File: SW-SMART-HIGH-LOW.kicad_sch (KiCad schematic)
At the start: 31 parts, among them IC1 MCP1416, J1 1 CTL IN, SW1 BTS50010-1TAD, SW2 VNB35N07xx-E, U1 STM32G071K8TxN, U2 NCV1117ST50, U3 NCV1117ST33, U4 MCP2562-E-SN

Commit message: fit a lot of stuff onto a small board
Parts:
- removed J1: 1 CTL IN, Connector_PinHeader_2.54mm:PinHeader_1x05_P2.54mm_Horizontal, symbol Connector_Generic:Conn_01x05
- removed U1: STM32G071K8TxN, Package_QFP:LQFP-32_7x7mm_P0.8mm, symbol MCU_ST_STM32G0:STM32G071K8TxN
- added CNRST1, CSTM2: 100n, Capacitor_SMD:C_0603_1608Metric_Pad1.08x0.95mm_HandSolder, symbol Device:C_Small
- added CSTM1: 4u7, Capacitor_SMD:C_0805_2012Metric_Pad1.18x1.45mm_HandSolder, symbol Device:C_Small
- added J1: H GND L, TerminalBlock_Phoenix:TerminalBlock_Phoenix_MKDS-1,5-3-5.08_1x03_P5.08mm_Horizontal, symbol Connector:Screw_Terminal_01x03
- added J2: SWLINK, symbol Connector_Generic:Conn_01x05
- added U1: STM32G0B1KBTx, Package_QFP:LQFP-32_7x7mm_P0.8mm, symbol MCU_ST_STM32G0:STM32G0B1KBTx
- renumbered RPD1 to R1
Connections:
- net +3.3V: now also CSTM1.1, CSTM2.1, J2.1 (Pin_1), U1.4 (VDD)
- net GND: now also CNRST1.2, CSTM1.2, CSTM2.2, J1.2 (Pin_2), J2.5 (Pin_5), U1.5 (VSS)
- net LOW_IN: no longer RIN2.1
- net SW1IN: no longer RIN1.1
- net SW1IS: no longer RIS_PROT1.1
- net CAN1_TX: now reaches U4.1 (TXD)
- net CAN1_TX: now also U1.23 (PA10/PA12)
- net CAN1_RX: now reaches U4.4 (RXD)
- net CAN1_RX: now also U1.22 (PA9/PA11)
- net CAN_L: now reaches U4.6 (CANL)
- net CAN_L: now also J1.3 (Pin_3)
- net CAN_H: now reaches U4.7 (CANH)
- net CAN_H: now also J1.1 (Pin_1)
- new net NRST: CNRST1.1, J2.2 (Pin_2), U1.6 (PF2)
- new net SWCLK: J2.3 (Pin_3), U1.25 (PA14)
- new net SWDIO: J2.4 (Pin_4), U1.24 (PA13)
- new net USART1_RX: U1.21 (PA10/UCPD1_DBCC2)
- new net USART1_TX: U1.19 (PA9/UCPD1_DBCC1)
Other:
- moved on the sheet: C3V1, C5V0, C5V1, U2, U3

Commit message: making progress on the layout
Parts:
- J1: renamed from J2; footprint (none) -> PCM_SparkFun-Connector:1x05_P2.54mm_Locking
- renumbered J1 to CAN1, U3 to VR3V3, U2 to VR5V0
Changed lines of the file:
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@@
 		(dnp no)
 		(fields_autoplaced yes)
-		(property "Reference" "J1"
+		(property "Reference" "CAN1"
 			(at 251.46 97.7899 0)
 			(effects
@@
 			(project ""
 				(path "/08d9f551-d314-4c5c-859f-da02a807087d"
-					(reference "J1")
+					(reference "CAN1")
 					(unit 1)
 				)
@@
 		(dnp no)
 		(fields_autoplaced yes)
-		(property "Reference" "U2"
+		(property "Reference" "VR5V0"
 			(at 38.1 69.85 0)
 			(effects
@@
 			(project ""
 				(path "/08d9f551-d314-4c5c-859f-da02a807087d"
-					(reference "U2")
+					(reference "VR5V0")
 					(unit 1)
 				)
@@
 		(dnp no)
 		(fields_autoplaced yes)
-		(property "Reference" "J2"
+		(property "Reference" "J1"
 			(at 248.92 26.6699 0)
 			(effects
@@
 			)
 		)
-		(property "Footprint" ""
+		(property "Footprint" "PCM_SparkFun-Connector:1x05_P2.54mm_Locking"
 			(at 246.38 27.94 0)
 			(effects
@@
 			(project ""
 				(path "/08d9f551-d314-4c5c-859f-da02a807087d"
-					(reference "J2")
+					(reference "J1")
 					(unit 1)
 				)
@@
 		(dnp no)
 		(fields_autoplaced yes)
-		(property "Reference" "U3"
+		(property "Reference" "VR3V3"
 			(at 71.12 69.85 0)
 			(effects
@@
 			(project ""
 				(path "/08d9f551-d314-4c5c-859f-da02a807087d"
-					(reference "U3")
-					(unit 1)
-				)
+					(reference "VR3V3")
+					(unit 1)
+				)

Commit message: needs a bit more work
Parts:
- added J2: USART1, PCM_SparkFun-Connector:1x04_P2.54mm_Locking, symbol Connector_Generic:Conn_01x04
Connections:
- net +3.3V: now also J2.1 (Pin_1)
- net GND: now also J2.4 (Pin_4)
- net USART1_RX: now also J2.3 (Pin_3)
- net USART1_TX: now also J2.2 (Pin_2)
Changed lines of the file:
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@@
 	)
 	(junction
+		(at 223.52 99.06)
+		(diameter 0)
+		(color 0 0 0 0)
+	)
+	(junction
 		(at 92.71 49.53)
 		(diameter 0)
@@
 	(wire
 		(pts
+			(xy 223.52 87.63) (xy 223.52 99.06)
+		)
+		(stroke
+			(width 0)
+			(type default)
+		)
+	)
+	(wire
+		(pts
 			(xy 248.92 114.3) (xy 248.92 124.46)
 		)
@@
 	(wire
 		(pts
+			(xy 241.3 85.09) (xy 243.84 85.09)
+		)
+		(stroke
+			(width 0)
+			(type default)
+		)
+	)
+	(wire
+		(pts
 			(xy 116.84 66.04) (xy 101.6 66.04)
 		)
@@
 	(wire
 		(pts
+			(xy 243.84 87.63) (xy 223.52 87.63)
+		)
+		(stroke
+			(width 0)
+			(type default)
+		)
+	)
+	(wire
+		(pts
 			(xy 213.36 71.12) (xy 217.17 71.12)
 		)
@@
 	(wire
 		(pts
+			(xy 241.3 82.55) (xy 243.84 82.55)
+		)
+		(stroke
+			(width 0)
+			(type default)
+		)
+	)
+	(wire
+		(pts
 			(xy 25.4 96.52) (xy 38.1 96.52)
 		)
@@
 	(wire
 		(pts
-			(xy 187.96 99.06) (xy 243.84 99.06)
+			(xy 243.84 80.01) (xy 242.57 80.01)
+		)
+		(stroke
+			(width 0)
+			(type default)
+		)
+	)
+	(wire
+		(pts
+			(xy 187.96 99.06) (xy 223.52 99.06)
 		)
 		(stroke
@@
 	(wire
 		(pts
+			(xy 223.52 99.06) (xy 243.84 99.06)
+		)
+		(stroke
+			(width 0)
+			(type default)
+		)
+	)
+	(wire
+		(pts
 			(xy 92.71 49.53) (xy 92.71 60.96)
 		)
@@
 	(wire
 		(pts
+			(xy 242.57 76.2) (xy 242.57 80.01)
+		)
+		(stroke
+			(width 0)
+			(type default)
+		)
+	)
+	(wire
+		(pts
 			(xy 69.85 115.57) (xy 74.93 115.57)
 		)
@@
 		)
 	)
+	(label "USART1_RX"
+		(at 241.3 85.09 180)
+		(effects
+			(font
+				(size 1.27 1.27)
+			)
+			(justify right bottom)
+		)
+	)
 	(label "CAN_H"
 		(at 240.03 96.52 180)
@@
 		)
 	)
+	(label "USART1_TX"
+		(at 241.3 82.55 180)
+		(effects
+			(font
+				(size 1.27 1.27)
+			)
+			(justify right bottom)
+		)
+	)
 	(label "NRST"
 		(at 156.21 40.64 180)
@@
 	)
 	(symbol
+		(lib_id "Connector_Generic:Conn_01x04")
+		(at 248.92 82.55 0)
+		(unit 1)
+		(exclude_from_sim no)
+		(in_bom yes)
+		(on_board yes)
+		(dnp no)
+		(fields_autoplaced yes)
+		(property "Reference" "J2"
+			(at 251.46 82.5499 0)
+			(effects
+				(font
+					(size 1.27 1.27)
+				)
+				(justify left)
+			)
+		)
+		(property "Value" "USART1"
+			(at 251.46 85.0899 0)
+			(effects
+				(font
+					(size 1.27 1.27)
+				)
+				(justify left)
+			)
+		)
+		(property "Footprint" "PCM_SparkFun-Connector:1x04_P2.54mm_Locking"
+			(at 248.92 82.55 0)
+			(effects
+				(font
+					(size 1.27 1.27)
+				)
+				(hide yes)
+			)
+		)
+		(property "Datasheet" "~"
+			(at 248.92 82.55 0)
+			(effects
+				(font
+					(size 1.27 1.27)
+				)
+				(hide yes)
+			)
+		)
+		(property "Description" "Generic connector, single row, 01x04, script generated (kicad-library-utils/schlib/autogen/connector/)"
+			(at 248.92 82.55 0)
+			(effects
+				(font
+					(size 1.27 1.27)
+				)
+				(hide yes)
+			)
+		)
+		(pin "2"
+		)
+		(pin "4"
+		)
+		(pin "1"
+		)
+		(pin "3"
+		)
+		(instances
+			(project ""
+				(path "/08d9f551-d314-4c5c-859f-da02a807087d"
+					(reference "J2")
+					(unit 1)
+				)
+			)
+		)
+	)
+	(symbol
 		(lib_id "power:GND")
 		(at 187.96 102.87 0)
@@
 					(unit 1)
 				)
+			)
+		)
+	)
+	(symbol
+		(lib_id "power:+3.3V")
+		(at 242.57 76.2 0)
+		(unit 1)
+		(exclude_from_sim no)
+		(in_bom yes)
+		(on_board yes)
+		(dnp no)
+		(fields_autoplaced yes)
+		(property "Reference" "#PWR021"
+			(at 242.57 80.01 0)
+			(effects
+				(font
+					(size 1.27 1.27)
+				)
+				(hide yes)
+			)
+		)
+		(property "Value" "+3.3V"
+			(at 242.57 71.12 0)
+			(effects
+				(font
+					(size 1.27 1.27)
+				)
+			)
+		)
+		(property "Footprint" ""
+			(at 242.57 76.2 0)
+			(effects
+				(font
+					(size 1.27 1.27)
+				)
+				(hide yes)
+			)
+		)
+		(property "Datasheet" ""
+			(at 242.57 76.2 0)
+			(effects
+				(font
+					(size 1.27 1.27)
+				)
+				(hide yes)
+			)
+		)
+		(property "Description" "Power symbol creates a global label with name \"+3.3V\""
+			(at 242.57 76.2 0)
+			(effects
+				(font
+					(size 1.27 1.27)
+				)
+				(hide yes)
+			)
+		)
+		(pin "1"
+		)
+		(instances
+			(project "SW-SMART-HIGH-LOW"
+				(path "/08d9f551-d314-4c5c-859f-da02a807087d"
+					(reference "#PWR021")
+					(unit 1)
+				)

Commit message: added voltage divider for +12v
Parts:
- added CDIV1, CIS1: 100n, Capacitor_SMD:C_0603_1608Metric_Pad1.08x0.95mm_HandSolder, symbol Device:C_Small
- added RVDIV1: 10K, Resistor_SMD:R_0603_1608Metric_Pad0.98x0.95mm_HandSolder, symbol Device:R_Small_US
- added RVDIV2: 4K7, Resistor_SMD:R_0603_1608Metric_Pad0.98x0.95mm_HandSolder, symbol Device:R_Small_US
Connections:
- net +12V: now also RVDIV1.2
- net GND: now also CDIV1.2, CIS1.2, RVDIV2.1
- net SW1IN: now also RIN1.1, U1.32 (PB8)
- net SW1IS: now also RIS_PROT1.1, U1.7 (PA0), CIS1.1
- net SW2IN: now reaches RIN2.1
- net SW2IN: now also U1.30 (PB6)
- net VS: now reaches U1.9 (PA2)
- net VS: now also CDIV1.1, RVDIV1.1, RVDIV2.2

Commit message: I think the layout is complete
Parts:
- renumbered R1 to RSTBY1
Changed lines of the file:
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@@
 		(on_board yes)
 		(dnp no)
-		(property "Reference" "R1"
+		(property "Reference" "RSTBY1"
 			(at 113.538 83.312 0)
 			(effects
@@
 			(project "SW-SMART-HIGH-LOW"
 				(path "/08d9f551-d314-4c5c-859f-da02a807087d"
-					(reference "R1")
+					(reference "RSTBY1")
 					(unit 1)
 				)

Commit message: added caps for gate drive IC
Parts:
- added CFET1: 100n, Capacitor_SMD:C_0603_1608Metric_Pad1.08x0.95mm_HandSolder, symbol Device:C_Small
- added CFET2: 1u, Capacitor_SMD:C_0805_2012Metric_Pad1.18x1.45mm_HandSolder, symbol Device:C_Small
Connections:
- net +12V: now also CFET1.1, CFET2.1
- net GND: now also CFET1.2, CFET2.2
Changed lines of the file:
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@@
 	)
 	(junction
+		(at 21.59 60.96)
+		(diameter 0)
+		(color 0 0 0 0)
+	)
+	(junction
 		(at 62.23 38.1)
 		(diameter 0)
@@
 	)
 	(junction
+		(at 21.59 38.1)
+		(diameter 0)
+		(color 0 0 0 0)
+	)
+	(junction
 		(at 92.71 29.21)
 		(diameter 0)
@@
 	)
 	(junction
+		(at 33.02 60.96)
+		(diameter 0)
+		(color 0 0 0 0)
+	)
+	(junction
 		(at 92.71 46.99)
 		(diameter 0)
@@
 	)
 	(junction
+		(at 33.02 38.1)
+		(diameter 0)
+		(color 0 0 0 0)
+	)
+	(junction
 		(at 123.19 22.86)
 		(diameter 0)
@@
 	(wire
 		(pts
+			(xy 21.59 38.1) (xy 21.59 45.72)
+		)
+		(stroke
+			(width 0)
+			(type default)
+		)
+	)
+	(wire
+		(pts
 			(xy 57.15 87.63) (xy 57.15 96.52)
 		)
@@
 	(wire
 		(pts
+			(xy 33.02 60.96) (xy 21.59 60.96)
+		)
+		(stroke
+			(width 0)
+			(type default)
+		)
+	)
+	(wire
+		(pts
 			(xy 160.02 132.08) (xy 160.02 135.89)
 		)
@@
 	(wire
 		(pts
+			(xy 17.78 38.1) (xy 17.78 40.64)
+		)
+		(stroke
+			(width 0)
+			(type default)
+		)
+	)
+	(wire
+		(pts
 			(xy 62.23 49.53) (xy 69.85 49.53)
 		)
@@
 	(wire
 		(pts
+			(xy 21.59 50.8) (xy 21.59 60.96)
+		)
+		(stroke
+			(width 0)
+			(type default)
+		)
+	)
+	(wire
+		(pts
 			(xy 236.22 25.4) (xy 241.3 25.4)
 		)
@@
 	(wire
 		(pts
+			(xy 21.59 60.96) (xy 17.78 60.96)
+		)
+		(stroke
+			(width 0)
+			(type default)
+		)
+	)
+	(wire
+		(pts
 			(xy 233.68 146.05) (xy 248.92 146.05)
 		)
@@
 	(wire
 		(pts
+			(xy 33.02 38.1) (xy 21.59 38.1)
+		)
+		(stroke
+			(width 0)
+			(type default)
+		)
+	)
+	(wire
+		(pts
 			(xy 48.26 73.66) (xy 48.26 81.28)
 		)
@@
 	(wire
 		(pts
+			(xy 21.59 38.1) (xy 17.78 38.1)
+		)
+		(stroke
+			(width 0)
+			(type default)
+		)
+	)
+	(wire
+		(pts
 			(xy 105.41 177.8) (xy 105.41 182.88)
 		)
@@
 	(wire
 		(pts
+			(xy 17.78 60.96) (xy 17.78 45.72)
+		)
+		(stroke
+			(width 0)
+			(type default)
+		)
+	)
+	(wire
+		(pts
 			(xy 113.03 109.22) (xy 113.03 113.03)
 		)
@@
 	)
 	(symbol
+		(lib_id "Device:C_Small")
+		(at 17.78 43.18 0)
+		(unit 1)
+		(exclude_from_sim no)
+		(in_bom yes)
+		(on_board yes)
+		(dnp no)
+		(fields_autoplaced yes)
+		(property "Reference" "CFET2"
+			(at 20.32 41.9162 0)
+			(effects
+				(font
+					(size 1.27 1.27)
+				)
+				(justify left)
+			)
+		)
+		(property "Value" "1u"
+			(at 20.32 44.4562 0)
+			(effects
+				(font
+					(size 1.27 1.27)
+				)
+				(justify left)
+			)
+		)
+		(property "Footprint" "Capacitor_SMD:C_0805_2012Metric_Pad1.18x1.45mm_HandSolder"
+			(at 17.78 43.18 0)
+			(effects
+				(font
+					(size 1.27 1.27)
+				)
+				(hide yes)
+			)
+		)
+		(property "Datasheet" "~"
+			(at 17.78 43.18 0)
+			(effects
+				(font
+					(size 1.27 1.27)
+				)
+				(hide yes)
+			)
+		)
+		(property "Description" "Low ESR film"
+			(at 17.78 43.18 0)
+			(effects
+				(font
+					(size 1.27 1.27)
+				)
+				(hide yes)
+			)
+		)
+		(pin "2"
+		)
+		(pin "1"
+		)
+		(instances
+			(project "SW-SMART-HIGH-LOW"
+				(path "/08d9f551-d314-4c5c-859f-da02a807087d"
+					(reference "CFET2")
+					(unit 1)
+				)
+			)
+		)
+	)
+	(symbol
 		(lib_id "Connector_Generic:Conn_01x05")
 		(at 246.38 27.94 0)
@@
 					(unit 1)
 				)
+			)
+		)
+	)
+	(symbol
+		(lib_id "Device:C_Small")
+		(at 21.59 48.26 0)
+		(unit 1)
+		(exclude_from_sim no)
+		(in_bom yes)
+		(on_board yes)
+		(dnp no)
+		(fields_autoplaced yes)
+		(property "Reference" "CFET1"
+			(at 24.13 46.9962 0)
+			(effects
+				(font
+					(size 1.27 1.27)
+				)
+				(justify left)
+			)
+		)
+		(property "Value" "100n"
+			(at 24.13 49.5362 0)
+			(effects
+				(font
+					(size 1.27 1.27)
+				)
+				(justify left)
+			)
+		)
+		(property "Footprint" "Capacitor_SMD:C_0603_1608Metric_Pad1.08x0.95mm_HandSolder"
+			(at 21.59 48.26 0)
+			(effects
+				(font
+					(size 1.27 1.27)
+				)
+				(hide yes)
+			)
+		)
+		(property "Datasheet" "~"
+			(at 21.59 48.26 0)
+			(effects
+				(font
+					(size 1.27 1.27)
+				)
+				(hide yes)
+			)
+		)
+		(property "Description" "Unpolarized capacitor, small symbol"
+			(at 21.59 48.26 0)
+			(effects
+				(font
+					(size 1.27 1.27)
+				)
+				(hide yes)
+			)
+		)
+		(pin "2"
+		)
+		(pin "1"
+		)
+		(instances
+			(project "SW-SMART-HIGH-LOW"
+				(path "/08d9f551-d314-4c5c-859f-da02a807087d"
+					(reference "CFET1")
+					(unit 1)
+				)

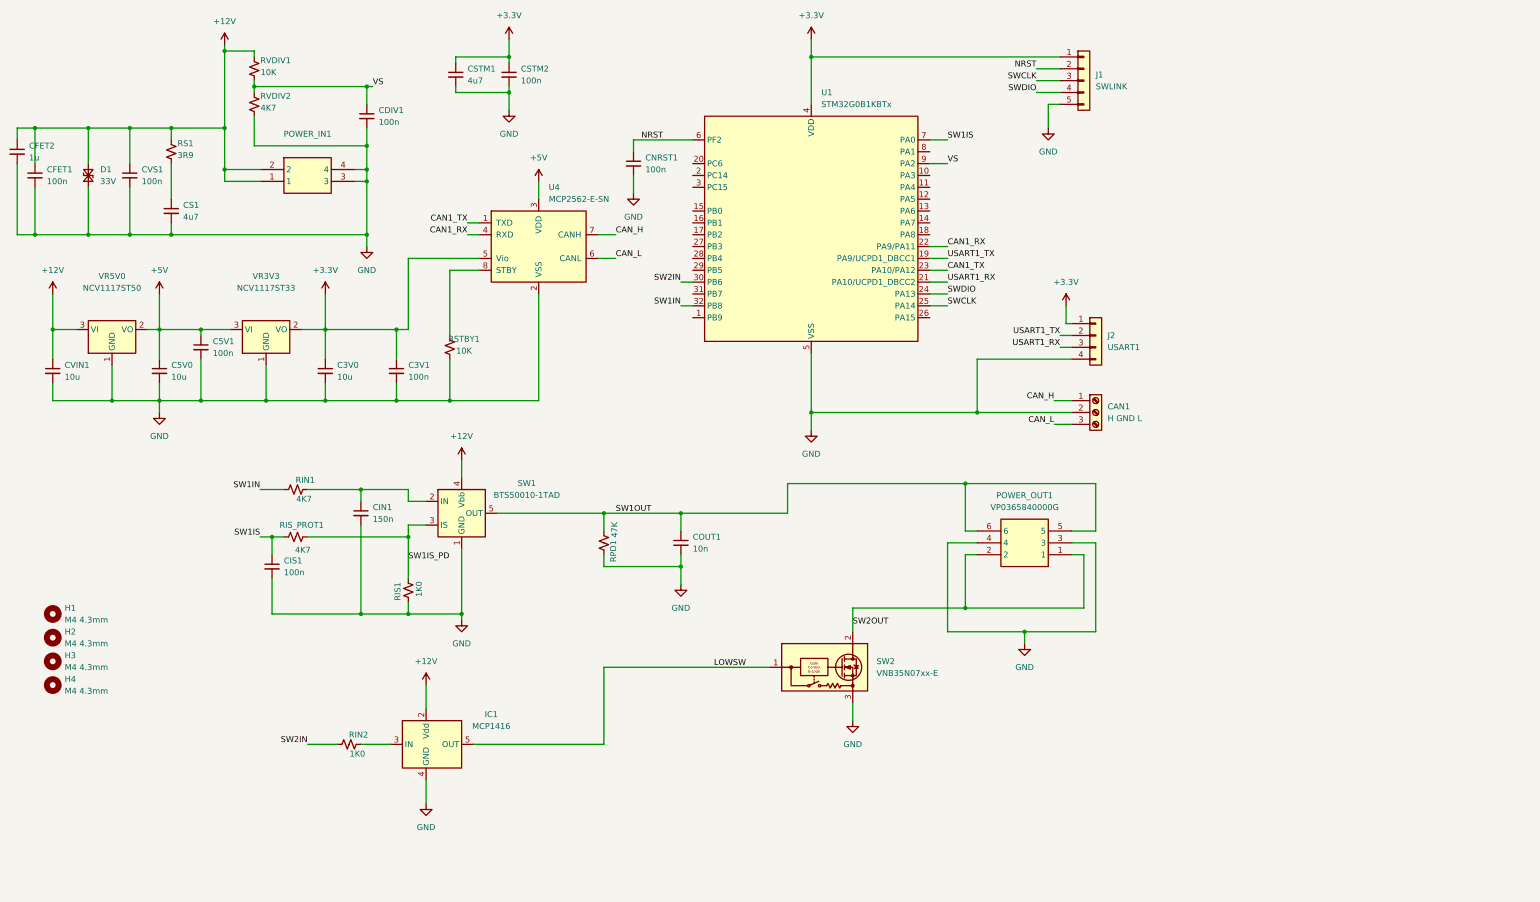
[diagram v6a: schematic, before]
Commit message: added 5v smps, needs layout fixed now
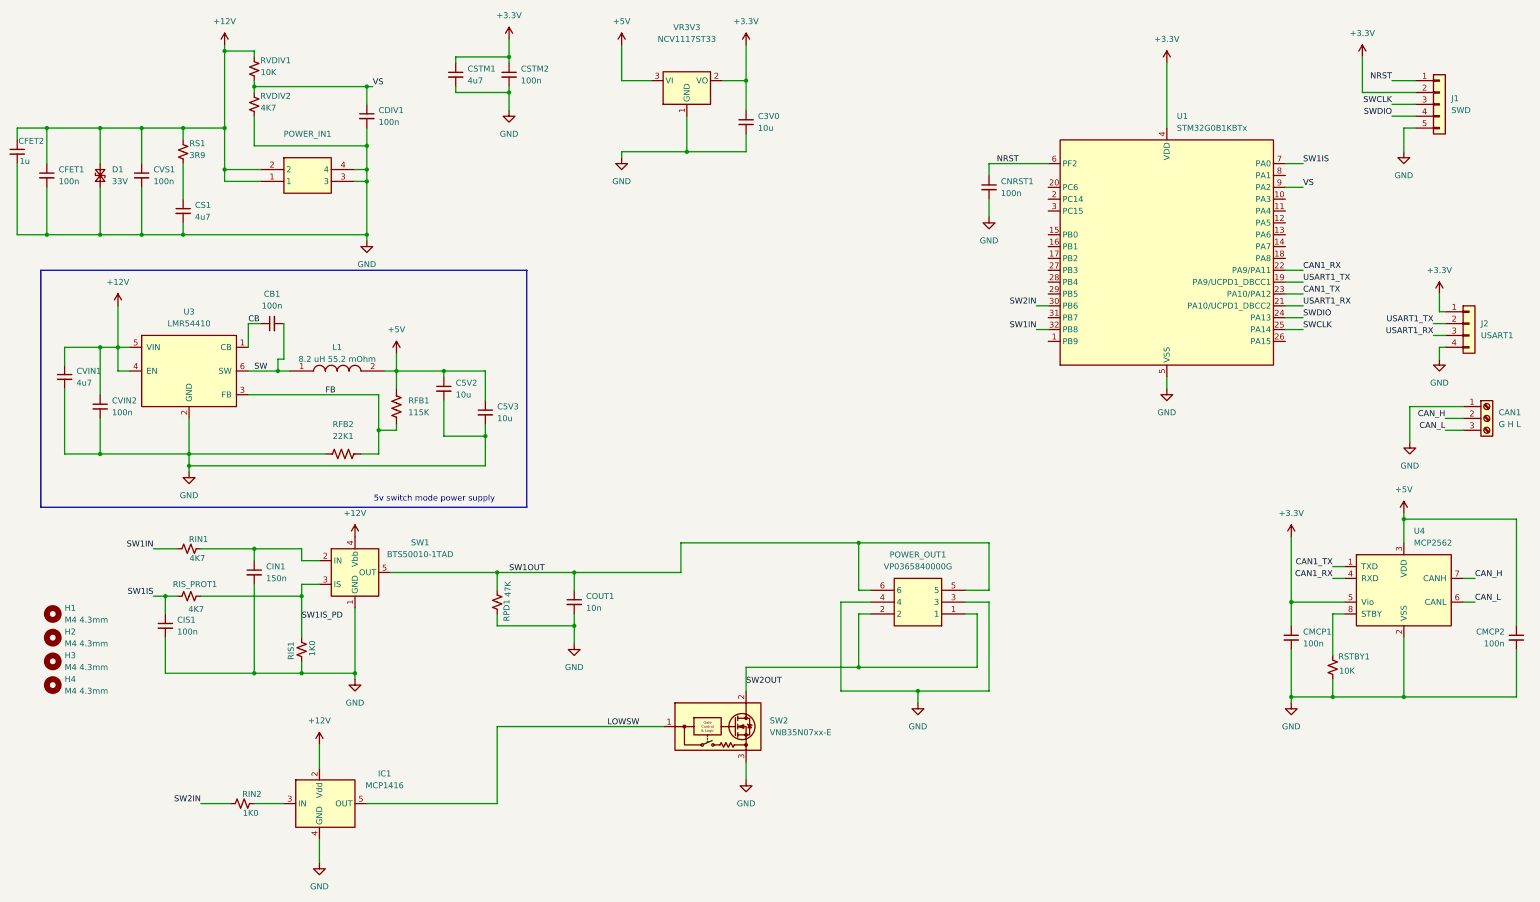
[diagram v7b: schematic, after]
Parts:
- removed C5V0: 10u, Capacitor_SMD:C_0805_2012Metric_Pad1.18x1.45mm_HandSolder, symbol Device:C_Small
- removed VR5V0: NCV1117ST50, PCM_SparkFun-Semiconductor-Standard:SOT-223-3_TabPin2, symbol PCM_SparkFun-Regulator:LM1117-3.3
- added C5V2, C5V3: 10u, Capacitor_SMD:C_0805_2012Metric_Pad1.18x1.45mm_HandSolder, symbol Device:C_Small
- added CB1, CVIN2: 100n, Capacitor_SMD:C_0603_1608Metric_Pad1.08x0.95mm_HandSolder, symbol Device:C_Small
- added L1: 8.2 uH 55.2 mOhm, SamacSys_Parts:SRP5030HMT2R2M, symbol SamacSys_Parts:SRP5030HMT-8R2M
- added RFB1: 115K, Resistor_SMD:R_0603_1608Metric_Pad0.98x0.95mm_HandSolder, symbol Device:R_US
- added RFB2: 22K1, Resistor_SMD:R_0603_1608Metric_Pad0.98x0.95mm_HandSolder, symbol Device:R_US
- added U3: LMR54410, Package_TO_SOT_SMD:SOT-23-6, symbol Regulator_Switching:LMR50410
- CAN1: value H GND L -> G H L
- CVIN1: value 10u -> 4u7; footprint Capacitor_SMD:C_1206_3216Metric_Pad1.33x1.80mm_HandSolder -> Capacitor_SMD:C_1210_3225Metric_Pad1.33x2.70mm_HandSolder
- J1: value SWLINK -> SWD
- U4: value MCP2562-E-SN -> MCP2562
- renumbered C3V1 to CMCP1, C5V1 to CMCP2
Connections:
- net +12V: now also CVIN2.1, U3.4 (EN), U3.5 (VIN)
- net +3.3V: now also J1.2 (Pin_2); no longer J1.1 (Pin_1)
- net +5V: now also C5V2.1, C5V3.1, L1.2, RFB1.1
- net CAN_H: now also CAN1.2 (Pin_2); no longer CAN1.1 (Pin_1)
- net GND: now also CAN1.1 (Pin_1), C5V2.2, C5V3.2, CVIN2.2, RFB2.1, U3.2 (GND); no longer CAN1.2 (Pin_2)
- net NRST: now also J1.1 (Pin_1); no longer J1.2 (Pin_2)
- new net CB: CB1.1, U3.1 (CB)
- new net FB: RFB1.2, RFB2.2, U3.3 (FB)
- new net SW: CB1.2, L1.1, U3.6 (SW)
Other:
- note added: "5v switch mode power supply"
- moved on the sheet: C3V0, CAN1, CFET1, CIN1, CIS1, CMCP1, CMCP2, CNRST1, COUT1, CS1, CVS1, D1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
